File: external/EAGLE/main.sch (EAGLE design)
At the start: 6 parts, among them IC1 AD590ZR, IC2 L293D, J1 1-794681-6, X2 332-02

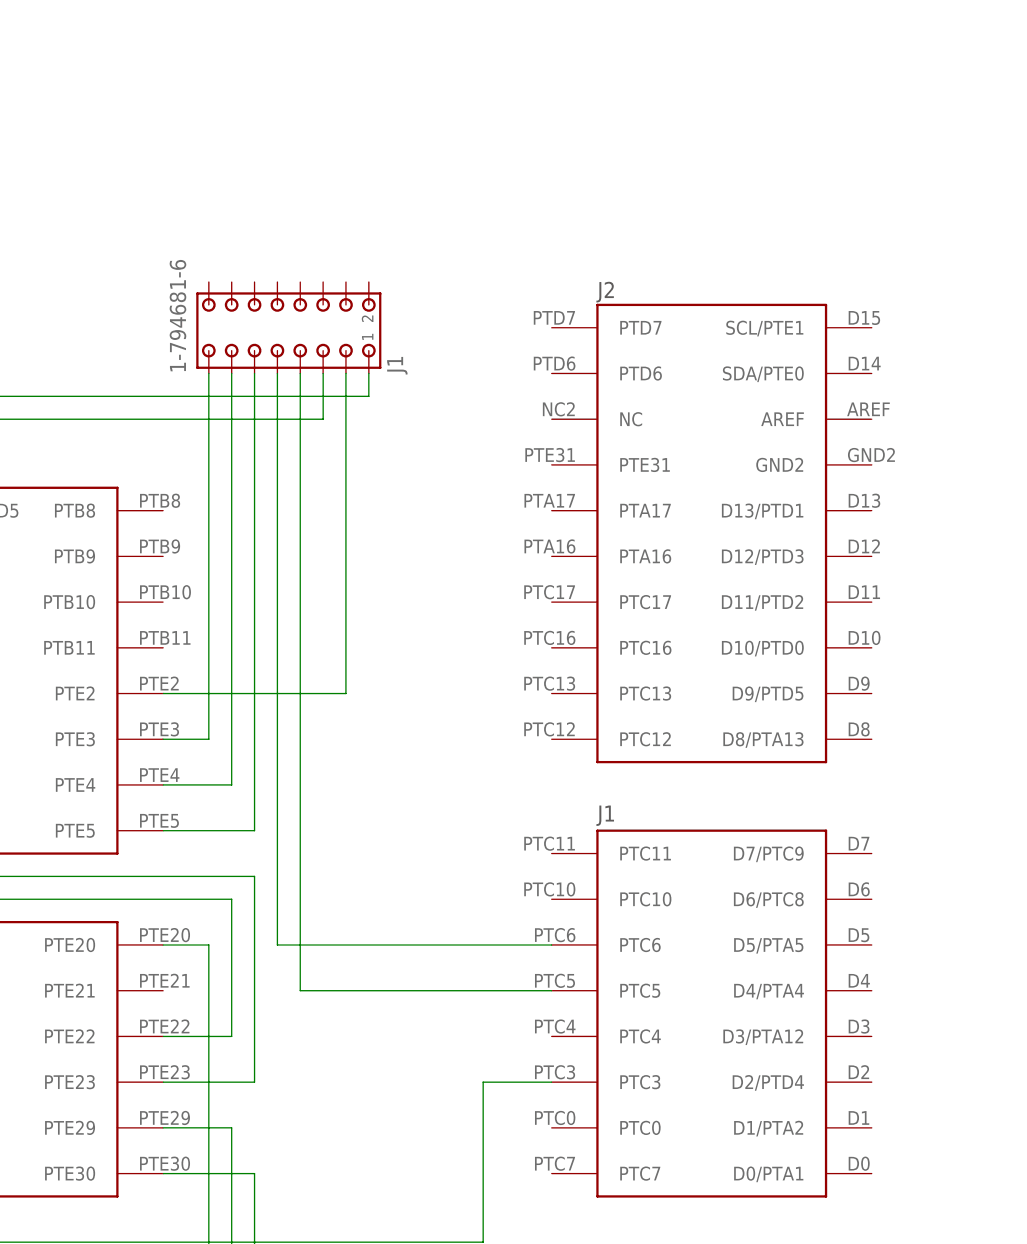
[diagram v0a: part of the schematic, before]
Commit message: Updating the schematic with the connections related to the keyboard. Also changed the header to the right one.
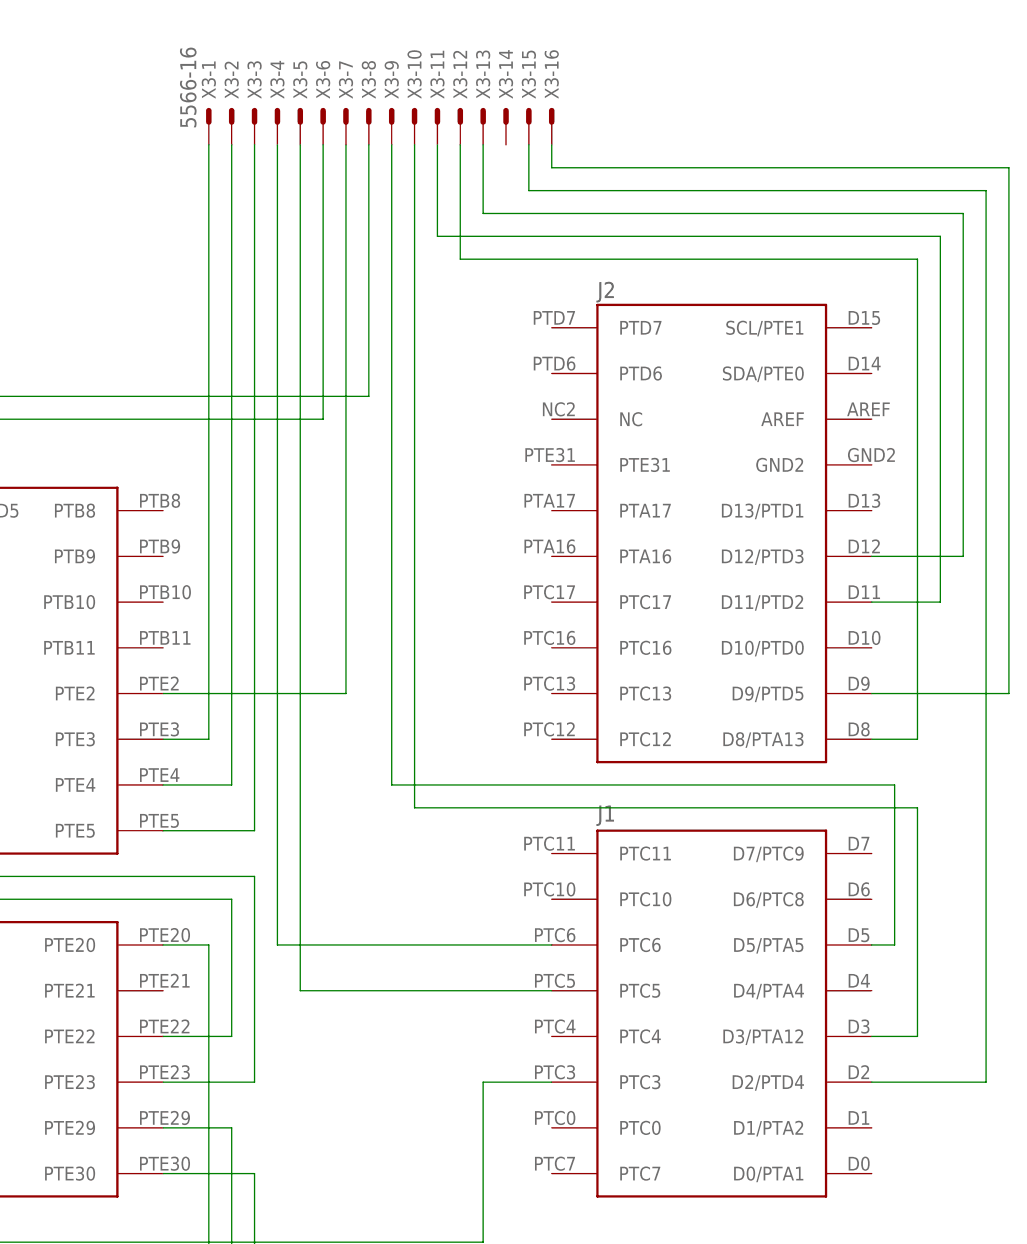
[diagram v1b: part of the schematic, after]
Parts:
- removed J1: 1-794681-6, con-amp:1-794681-6
- added X3: 5566-16, con-molex:5566-16
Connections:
- new net N$18: FRDM1.D5/PTA5, X3-9.S
- new net N$19: FRDM1.D3/PTA12, X3-10.S
- new net N$20: FRDM1.D8/PTA13, X3-12.S
- new net N$21: FRDM1.D11/PTD2, X3-11.S
- new net N$22: FRDM1.D12/PTD3, X3-13.S
- new net N$23: FRDM1.D2/PTD4, X3-15.S
- new net N$24: FRDM1.D9/PTD5, X3-16.S
- net N$11: now also X3-8.S; no longer J1.1
- net N$12: now also X3-1.S; no longer J1.15
- net N$13: now also X3-3.S; no longer J1.11
- net N$14: now also X3-2.S; no longer J1.13
- net N$15: now also X3-7.S; no longer J1.3
- net N$16: now also X3-4.S; no longer J1.9
- net N$17: now also X3-5.S; no longer J1.7
- net N$6: now also X3-6.S; no longer J1.5
